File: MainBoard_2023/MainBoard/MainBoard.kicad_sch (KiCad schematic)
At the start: 45 parts

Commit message: メイン基板設計一段落
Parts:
- added R?: 4.7k, symbol Device:R_Small
- added R?: 2.2k, symbol Device:R_Small
- added R?: 10k, symbol Device:R_Small
- added S? (x3): B3AL, B3AL1002PMS, symbol B3AL-1002P-MS:B3AL-1002P-MS
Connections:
- net +3.3V: now also R?.1
- net GND: now also S?.2, S?.2, S?.2
- net SWITCH: now reaches U?.34 (GP28)
- net SWITCH: now also R?.1, R?.2, S?.1
- new net: R?.1, R?.2, S?.1
- new net: R?.2, S?.1
- no-connect marks 40 -> 39
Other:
- moved on the sheet: C?, J?, R?, U?

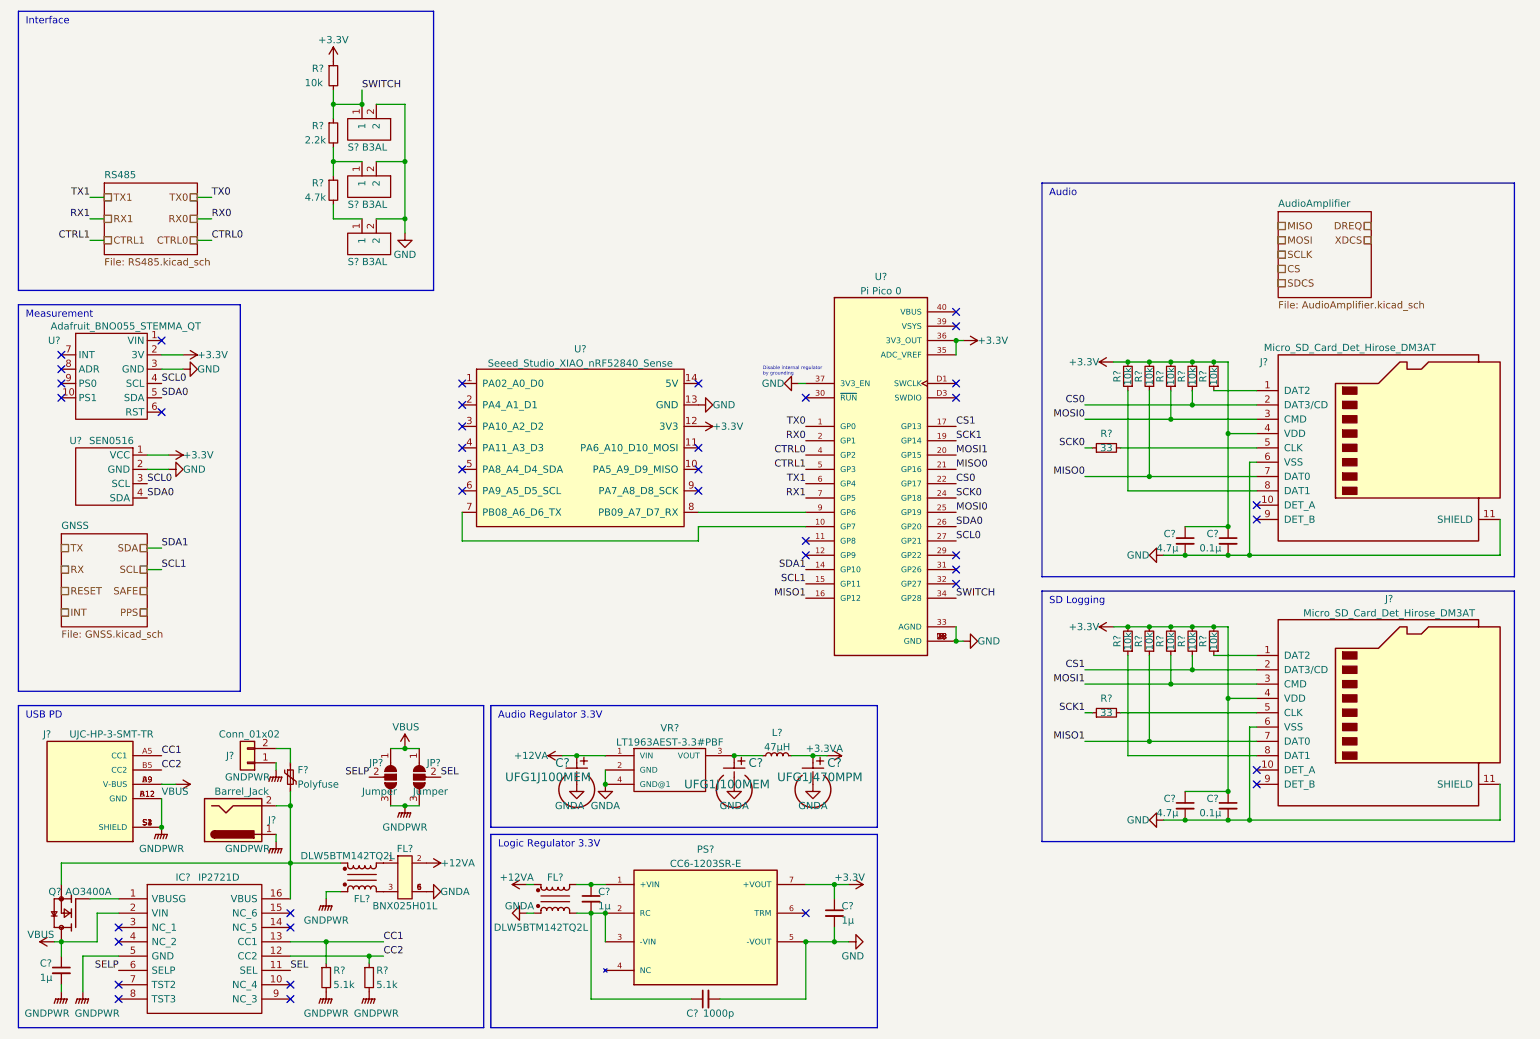
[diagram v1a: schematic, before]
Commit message: YDA142のフットプリントを作成
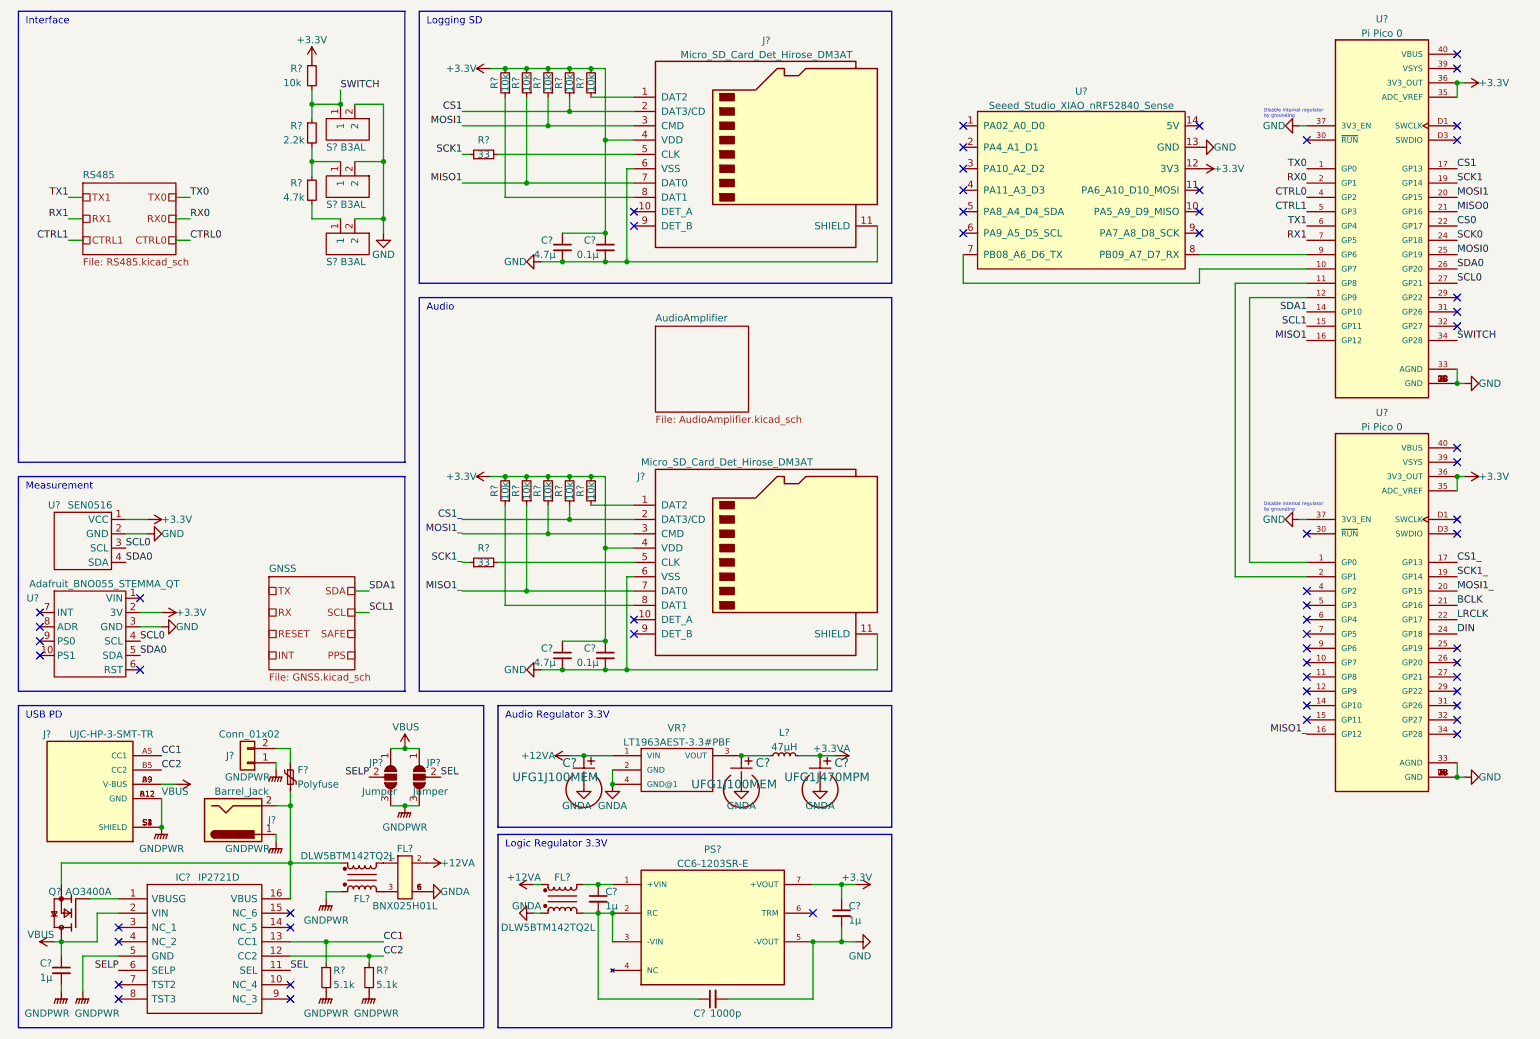
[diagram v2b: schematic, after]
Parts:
- added U?: Pi Pico 0, MODULE_SC0915, symbol Raspberry_Pi_Pico:SC0915
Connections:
- net +3.3V: now also U?.35 (ADC_VREF), U?.36 (3V3_OUT)
- net CS0: no longer J?.2 (DAT3/CD), R?.1
- net GND: now also U?.13 (GND), U?.18 (GND), U?.23 (GND), U?.28 (GND), U?.3 (GND), U?.33 (AGND), U?.37 (3V3_EN), U?.38 (GND), U?.8 (GND), U?.D2 (GND)
- net MISO0: no longer J?.7 (DAT0), R?.1
- net MOSI0: no longer J?.3 (CMD), R?.1
- net SCK0: no longer R?.1
- net at U?.11 (GP8): now also U?.2 (GP1)
- net at U?.12 (GP9): now also U?.1 (GP0)
- new net BCLK: U?.21 (GP16)
- new net CS1_: J?.2 (DAT3/CD), R?.1, U?.17 (GP13)
- new net DIN: U?.24 (GP18)
- new net LRCLK: U?.22 (GP17)
- new net MISO1_: J?.7 (DAT0), R?.1, U?.16 (GP12)
- new net MOSI1_: J?.3 (CMD), R?.1, U?.20 (GP15)
- new net SCK1_: R?.1, U?.19 (GP14)
- no-connect marks 39 -> 59
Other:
- note added: "Logging SD"
- note removed: "SD Logging"
- moved on the sheet: C?, FL?, J?, L?, PS?, R?, S?, U?, VR?

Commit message: アンプ回路
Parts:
- removed C? (x2): 1μ, symbol Device:C_Small
- removed C?: 1000p, Capacitor_SMD:C_0603_1608Metric_Pad1.08x0.95mm_HandSolder, symbol Device:C_Small
- removed FL?: DLW5BTM142TQ2L, FIL_DLW5BTM142TQ2L, symbol DLW5BTM142TQ2:DLW5BTM142TQ2L
- removed PS?: CC6-1203SR-E, CONV_CC6-1203SR-E, symbol CC6-1203SR-E:CC6-1203SR-E
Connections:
- net GNDA is gone; now on net GND: C?.2, C?.2, C?.2, FL?.4, FL?.5, FL?.6, VR?.2 (GND), VR?.4 (GND@1)
- net +12VA renamed +12V
- no-connect marks 59 -> 58
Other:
- note added: "Regulator 3.3V"
- note removed: "Audio Regulator 3.3V"
- note removed: "Logic Regulator 3.3V"
- moved on the sheet: C?, L?, VR?

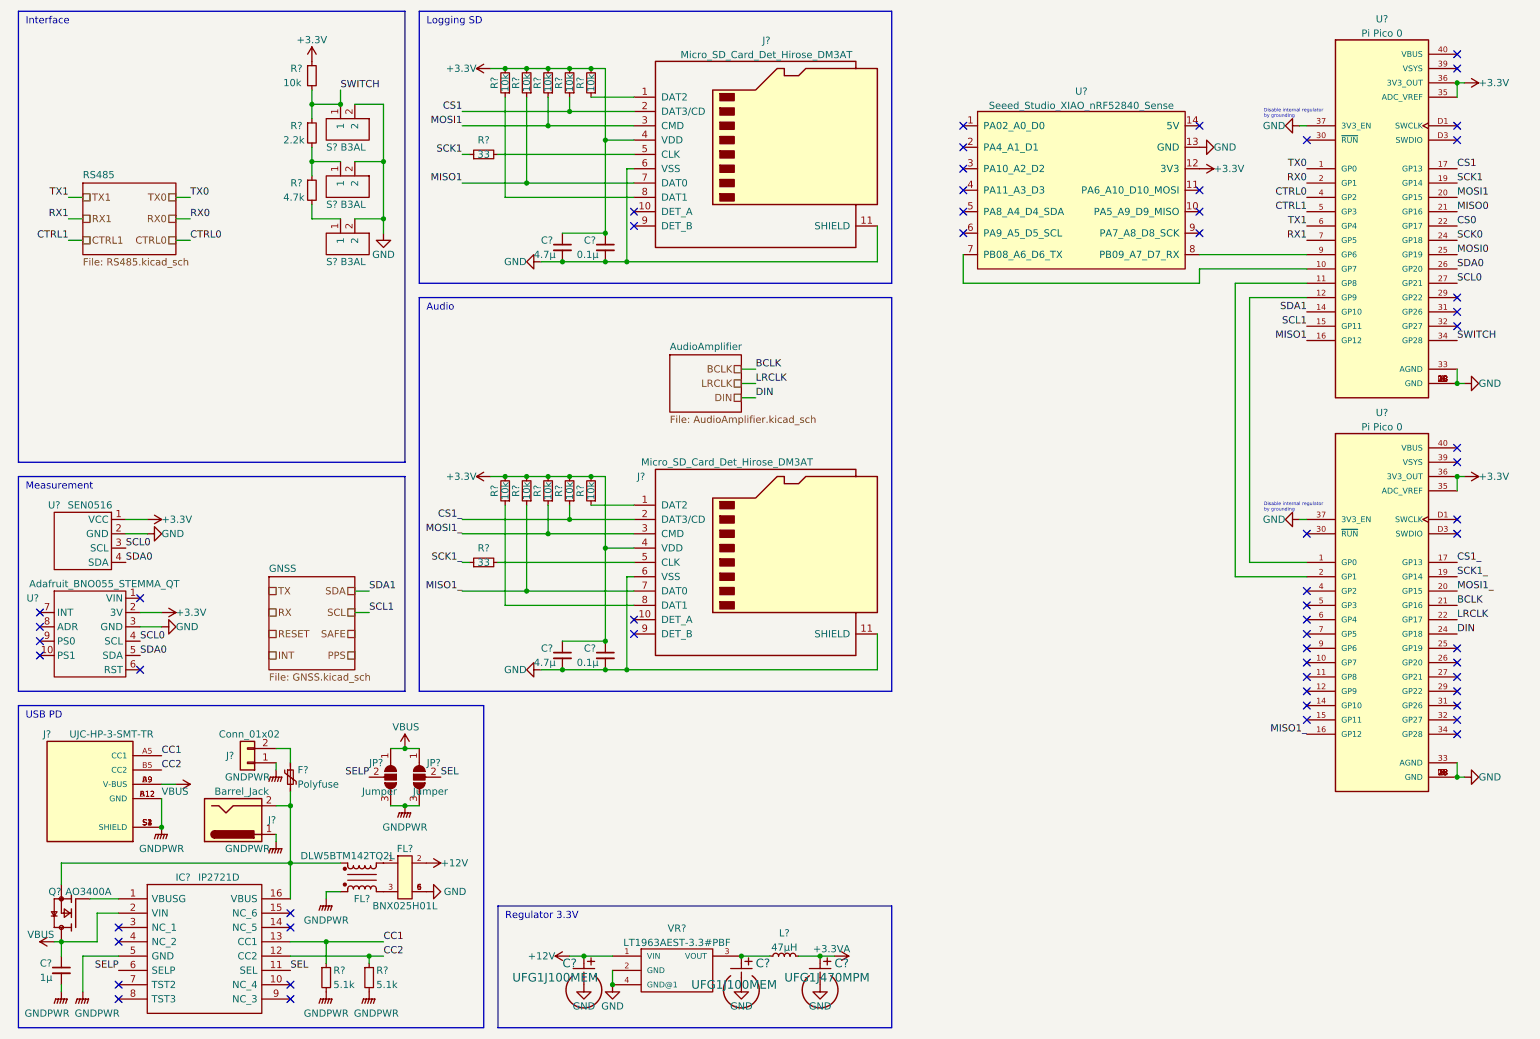
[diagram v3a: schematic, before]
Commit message: 回路だいたい完成
電解コンデンサのシンボルとフットプリントをkicad付属のものにする
ADCのピンと、SPIのOLEDのピンを共用にする
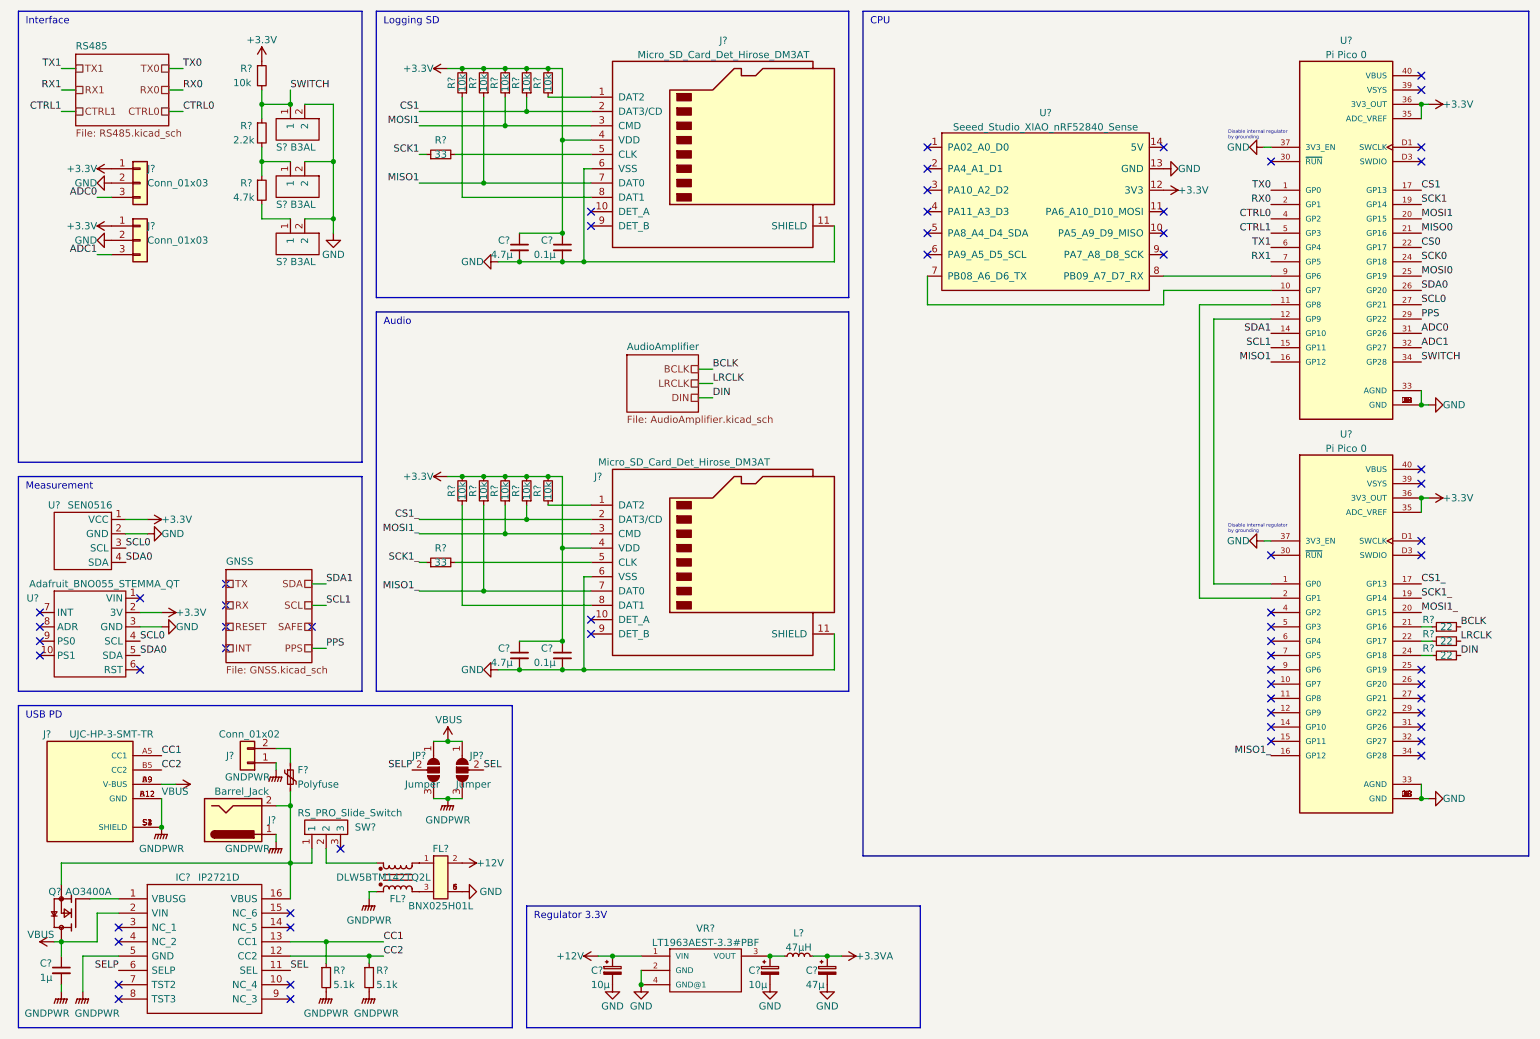
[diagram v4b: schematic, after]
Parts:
- removed C? (x2): UFG1J100MEM, PCAP_6_3x11THRU-ELECT_NCA, symbol UFG1J100MEM:UFG1J100MEM
- removed C?: UFG1J470MPM, PCAP_10x12_5-THRU-ELECT_NCA, symbol UFG1J470MPM:UFG1J470MPM
- added C? (x2): 10μ, symbol Device:C_Polarized_Small
- added C?: 47μ, symbol Device:C_Polarized_Small
- added J? (x2): Conn_01x03, symbol Connector_Generic:Conn_01x03
- added R? (x3): 22, symbol Device:R_Small
- added SW?: RS_PRO_Slide_Switch, symbol RS_PRO_PCB_Slide_Switch_SPDT_Latching_3A_120V_ac_Top:RS_PRO_PCB_Slide_Switch_SP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
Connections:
- net +12V: now also C?.1
- net +3.3V: now also J?.1 (Pin_1), J?.1 (Pin_1)
- net +3.3VA: now also C?.1
- net BCLK: now also R?.2; no longer U?.21 (GP16)
- net DIN: now also R?.2; no longer U?.24 (GP18)
- net GND: now also C?.2, C?.2, C?.2, J?.2 (Pin_2), J?.2 (Pin_2)
- net LRCLK: now also R?.2; no longer U?.22 (GP17)
- net PPS: now also U?.29 (GP22)
- net ADC0: now reaches U?.31 (GP26)
- net ADC0: now also J?.3 (Pin_3)
- net ADC1: now reaches U?.32 (GP27)
- net ADC1: now also J?.3 (Pin_3)
- net at F?.2, IC?.16 (VBUS), J?.2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: now also SW?.1; no longer FL?.1
- net at L?.1, VR?.3 (VOUT): now also C?.1
- new net: FL?.1, SW?.2
- new net: R?.1, U?.21 (GP16)
- new net: R?.1, U?.22 (GP17)
- new net: R?.1, U?.24 (GP18)
- no-connect marks 58 -> 61
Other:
- note added: "CPU"
- moved on the sheet: C?, FL?, J?, JP?, L?, R?, S?, U?, VR?

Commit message: 回路図完成
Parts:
- removed J?: Conn_01x03, symbol Connector_Generic:Conn_01x03
- added R?: 8.2k, symbol Device:R_Small
- added R?: 1.8k, symbol Device:R_Small
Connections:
- net ADC1 is gone; now on net ADC0: U?.32 (GP27)
- net +12V: now also R?.1, R?.1, R?.2
- net ADC0: no longer U?.31 (GP26)
- net GND: now also R?.2
- net PPS: now also U?.31 (GP26); no longer U?.29 (GP22)
- net CS0 renamed CS
- net MISO0 renamed MISO
- net MOSI0 renamed MOSI
- net SCK0 renamed SCK
- new net DRDY: U?.29 (GP22)
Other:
- added sheet ADC (ADC.kicad_sch)
- moved on the sheet: C?, FL?, J?, R?, U?

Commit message: ERC通った
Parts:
- gave numbers to parts that had none: 54
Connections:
- net +3.3VA is gone; now on net +3.3V: C8.1, L1.2
- net +12V: no longer R4.2, R5.1
- net CS renamed CS0
- net MISO renamed MISO0
- net MOSI renamed MOSI0
- net SCK renamed SCK0
- net SCL renamed SCL1
- net SDA renamed SDA1
- new net ADC/VBAT: R4.2, R5.1
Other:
- sheet ADC ports: added CS, DRDY, MISO, MOSI, SCK, VBAT; removed none
- sheet AudioAmplifier ports: added BCLK, DIN, LRCLK; removed none
- sheet GNSS ports: added INT, PPS, RESET, RX, SAFE, SCL, SDA, TX; removed none
- sheet RS485 ports: added CTRL0, CTRL1, RX0, RX1, TX0, TX1; removed none
